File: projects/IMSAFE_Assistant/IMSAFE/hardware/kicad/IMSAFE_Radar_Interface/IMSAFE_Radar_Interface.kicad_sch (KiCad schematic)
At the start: 0 parts

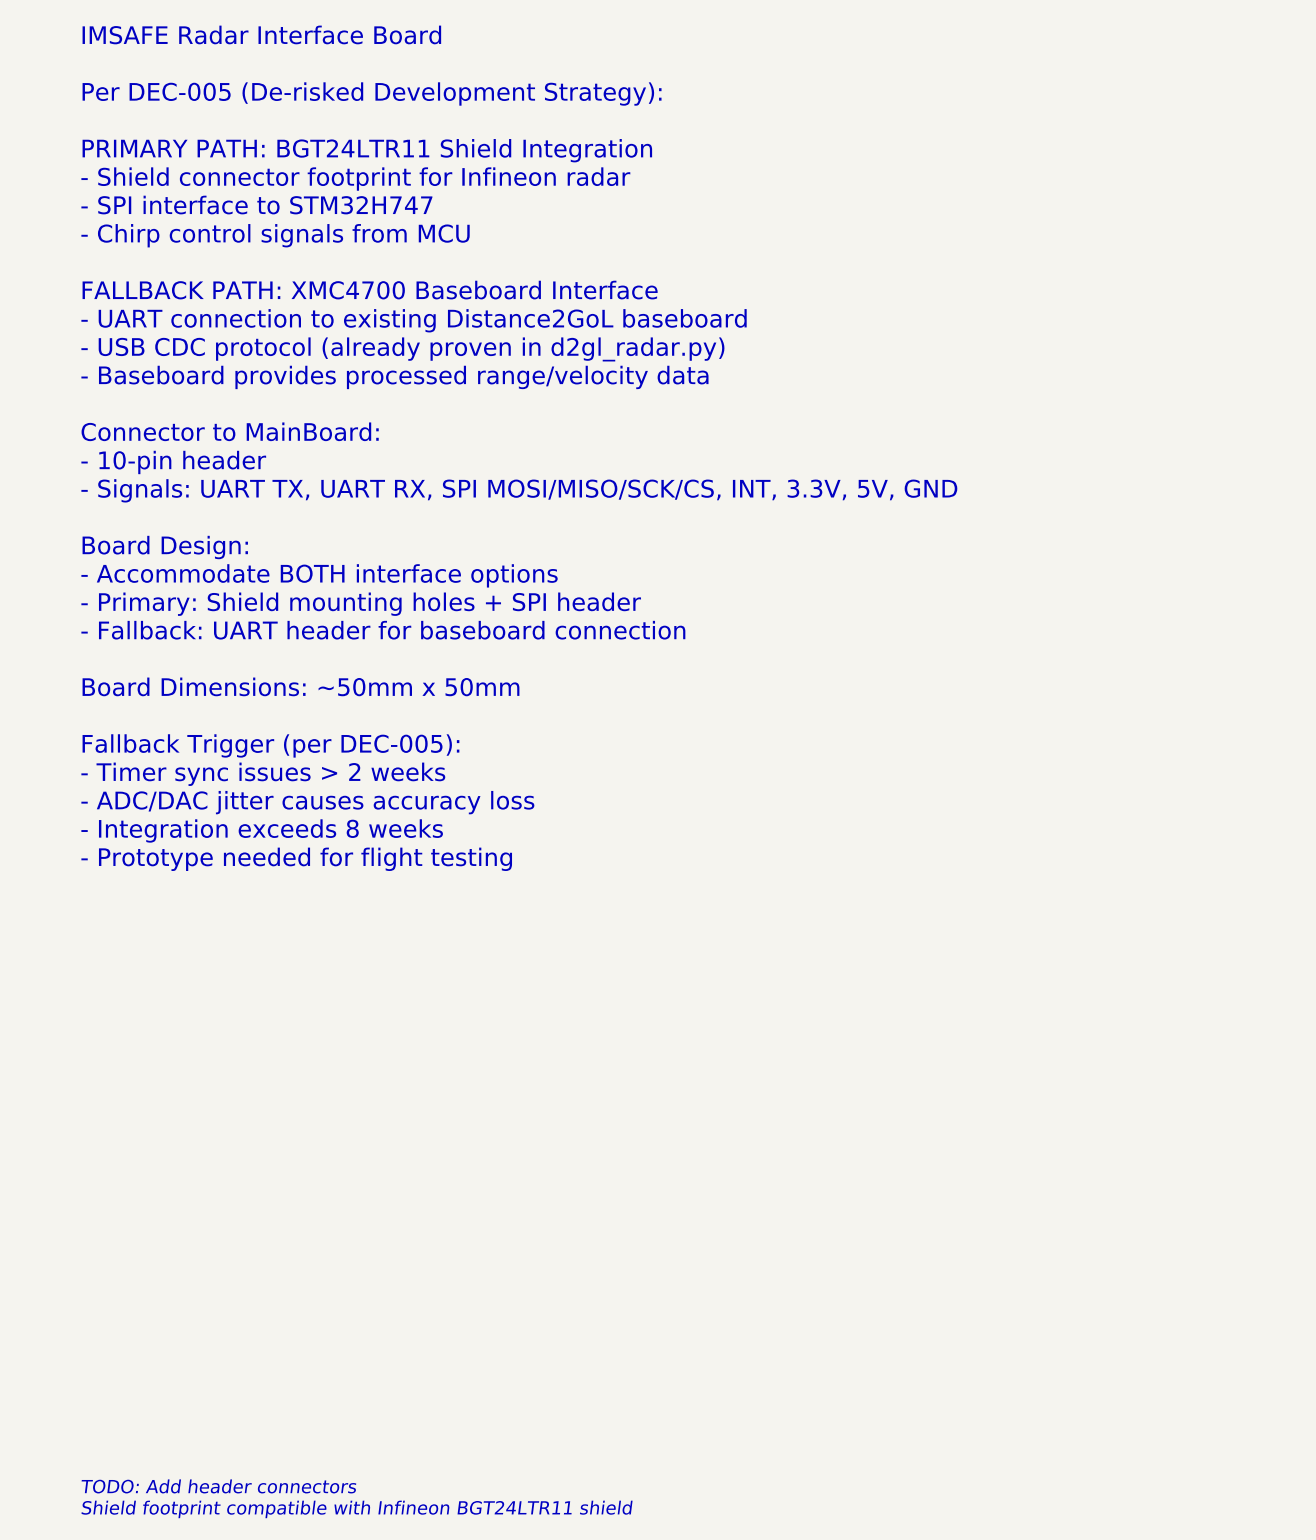
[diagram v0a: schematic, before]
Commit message: Update KiCad schematics and add analysis files
- Update all MainBoard schematic sections with component placement
- Add ERC reports and analysis scripts for schematic validation
- Update Radar Interface and SwitchLED Board projects
- Sync KiCad project files with latest session changes

Co-Authored-By: Claude Opus 4.5 <noreply@anthropic.com>
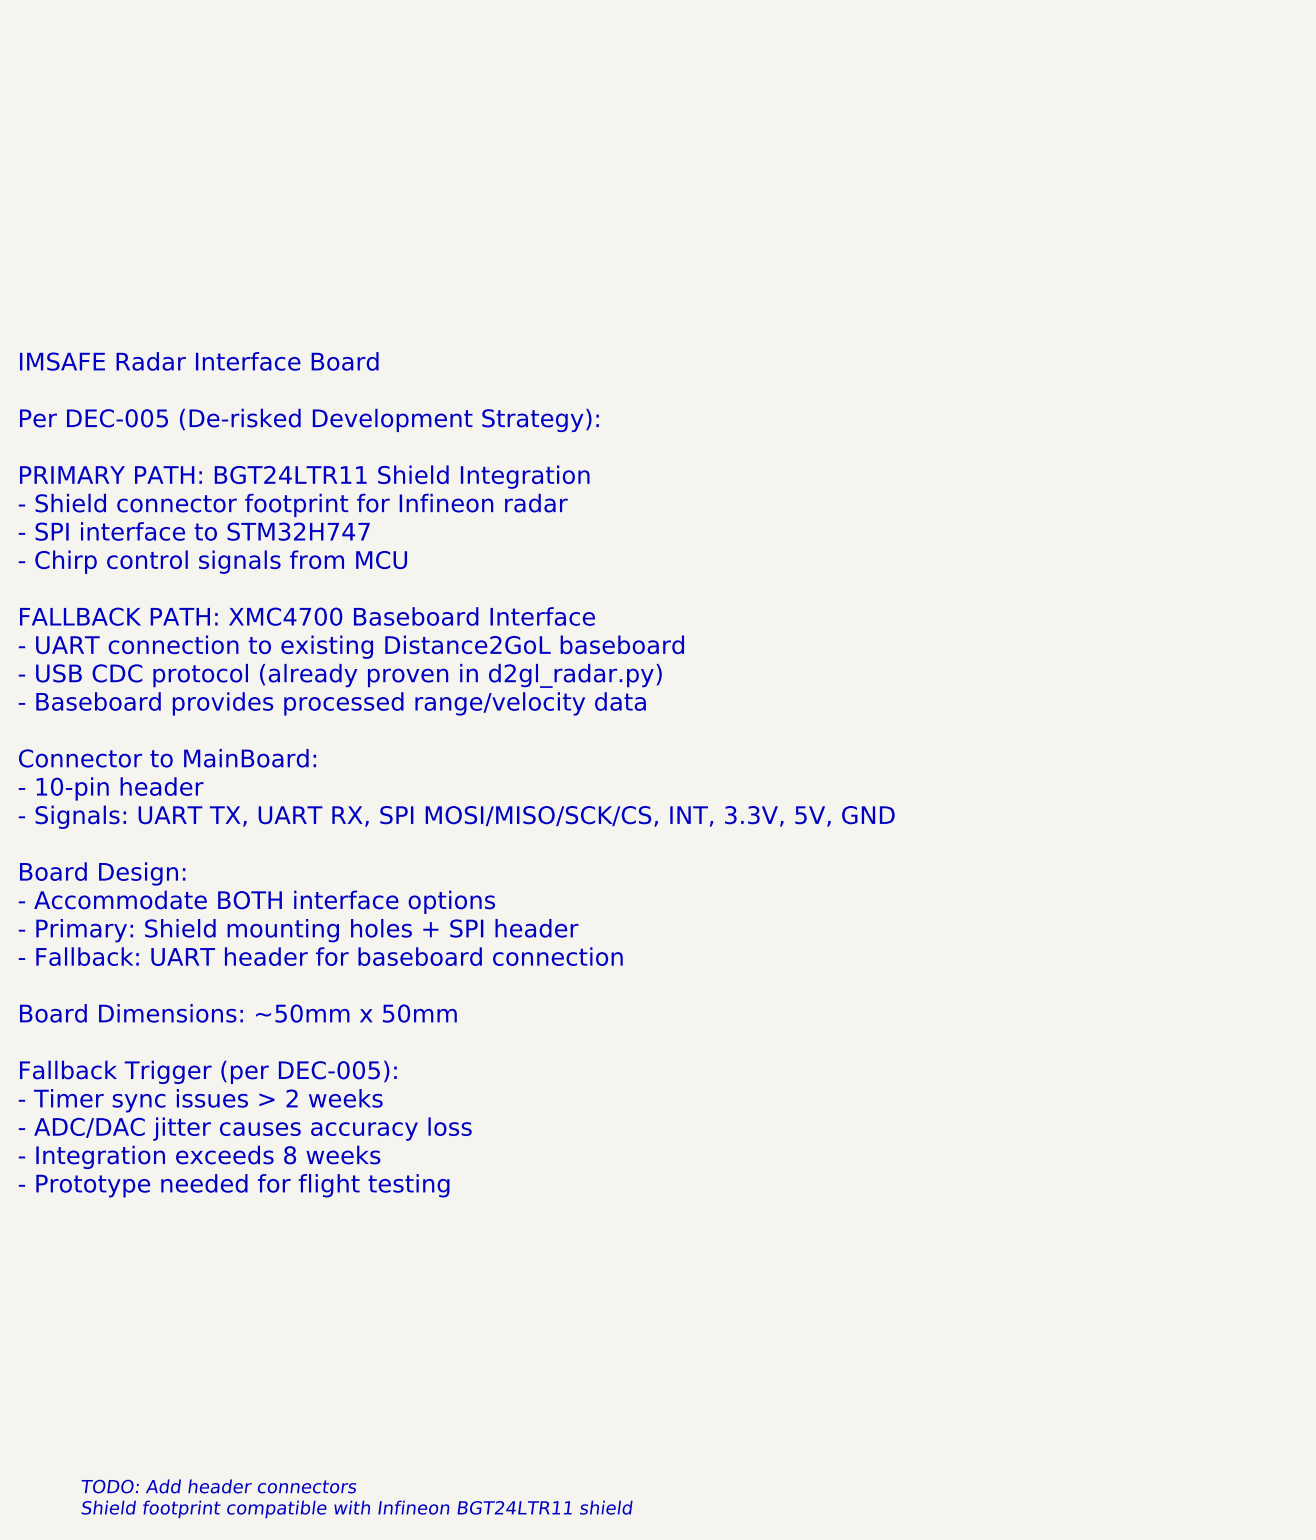
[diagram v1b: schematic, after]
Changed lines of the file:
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@@
 (kicad_sch
-	(version 20231120)
+	(version 20250114)
 	(generator "eeschema")
-	(generator_version "8.0")
-	(uuid "radar-root-0001-0002-000000000001")
+	(generator_version "9.0")
 	(paper "A4")
 	(title_block
@@
 		(comment 1 "BGT24LTR11 Integration / XMC4700 Fallback")
 		(comment 2 "Per DEC-005 De-risked Strategy")
-	)
-	(text "IMSAFE Radar Interface Board\n\nPer DEC-005 (De-risked Development Strategy):\n\nPRIMARY PATH: BGT24LTR11 Shield Integration\n- Shield connector footprint for Infineon radar\n- SPI interface to STM32H747\n- Chirp control signals from MCU\n\nFALLBACK PATH: XMC4700 Baseboard Interface\n- UART connection to existing Distance2GoL baseboard\n- USB CDC protocol (already proven in d2gl_radar.py)\n- Baseboard provides processed range/velocity data\n\nConnector to MainBoard:\n- 10-pin header\n- Signals: UART TX, UART RX, SPI MOSI/MISO/SCK/CS, INT, 3.3V, 5V, GND\n\nBoard Design:\n- Accommodate BOTH interface options\n- Primary: Shield mounting holes + SPI header\n- Fallback: UART header for baseboard connection\n\nBoard Dimensions: ~50mm x 50mm\n\nFallback Trigger (per DEC-005):\n- Timer sync issues > 2 weeks\n- ADC/DAC jitter causes accuracy loss\n- Integration exceeds 8 weeks\n- Prototype needed for flight testing"
-		(exclude_from_sim no)
-		(at 25.4 25.4 0)
-		(effects
-			(font
-				(size 2 2)
-			)
-			(justify left)
-		)
-		(uuid "radar-text-001")
 	)
 	(text "TODO: Add header connectors\nShield footprint compatible with Infineon BGT24LTR11 shield"
@@
 			(justify left)
 		)
-		(uuid "radar-todo-001")
 	)
+	(text "IMSAFE Radar Interface Board\n\nPer DEC-005 (De-risked Development Strategy):\n\nPRIMARY PATH: BGT24LTR11 Shield Integration\n- Shield connector footprint for Infineon radar\n- SPI interface to STM32H747\n- Chirp control signals from MCU\n\nFALLBACK PATH: XMC4700 Baseboard Interface\n- UART connection to existing Distance2GoL baseboard\n- USB CDC protocol (already proven in d2gl_radar.py)\n- Baseboard provides processed range/velocity data\n\nConnector to MainBoard:\n- 10-pin header\n- Signals: UART TX, UART RX, SPI MOSI/MISO/SCK/CS, INT, 3.3V, 5V, GND\n\nBoard Design:\n- Accommodate BOTH interface options\n- Primary: Shield mounting holes + SPI header\n- Fallback: UART header for baseboard connection\n\nBoard Dimensions: ~50mm x 50mm\n\nFallback Trigger (per DEC-005):\n- Timer sync issues > 2 weeks\n- ADC/DAC jitter causes accuracy loss\n- Integration exceeds 8 weeks\n- Prototype needed for flight testing"
+		(exclude_from_sim no)
+		(at 18.288 62.484 0)
+		(effects
+			(font
+				(size 2 2)
+			)
+			(justify left)
+		)
+	)
+	(sheet_instances
+		(path "/"
+			(page "1")
+		)
+	)
+	(embedded_fonts no)
 )
